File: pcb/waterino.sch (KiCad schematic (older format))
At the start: 40 parts, among them CON1 BARREL_JACK, IC1 ATMEGA168A-P, P1 CONN_02X02, P2 CONN_01X06, P3 CONN_01X07, P4 CONN_01X04, P5 CONN_01X07, SW1 SW_PUSH, U1 MAX6817, U2 LM7805CT, U3 MIC94090, Y1 Crystal

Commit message: wip
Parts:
- removed C8: 22pF, Capacitors_SMD:C_1206_HandSoldering, symbol C
- removed D6, D7: D, Diodes_ThroughHole:D_DO-41_SOD81_P7.62mm_Horizontal, symbol D
- removed IC1: ATMEGA168A-P, Housings_DIP:DIP-28_W7.62mm_Socket, symbol ATMEGA168A-P
- removed P2: CONN_01X06, Pin_Headers:Pin_Header_Straight_1x06_Pitch2.54mm, symbol CONN_01X06
- removed P3: CONN_01X07, Pin_Headers:Pin_Header_Angled_1x07_Pitch2.54mm, symbol CONN_01X07
- removed R10: 1M, Resistors_SMD:R_1206_HandSoldering, symbol R
- removed R6: 150R, Resistors_SMD:R_1206_HandSoldering, symbol R
- removed U1: MAX6817, TO_SOT_Packages_SMD:SOT-23-6_Handsoldering, symbol MAX6817
- removed Y1: Crystal, Crystals:Crystal_HC49-U_Vertical, symbol Crystal
- added C11: 100nF, Capacitors_SMD:C_1206_HandSoldering, symbol C
- added C12: 10nF, Capacitors_SMD:C_1206_HandSoldering, symbol C
- added D2: D_Schottky_AKA, TO_SOT_Packages_SMD:TO-252-2_Rectifier, symbol D_Schottky_AKA
- added D3, D5: D_Schottky, Diodes_SMD:D_SOD-123, symbol D_Schottky
- added J1: ICSP, Pin_Headers:Pin_Header_Straight_2x03_Pitch2.54mm, symbol CONN_02X03
- added J2: EXT_B, Pin_Headers:Pin_Header_Angled_1x06_Pitch2.54mm, symbol CONN_01X06
- added J3: EXT_A, Pin_Headers:Pin_Header_Angled_1x12_Pitch2.54mm, symbol CONN_01X12
- added R2: 4k7, Resistors_SMD:R_1206_HandSoldering, symbol R
- added R3, R4: 150, Resistors_SMD:R_1206_HandSoldering, symbol R
- added U3: ATMEGA168-20AU, Housings_QFP:TQFP-32_7x7mm_Pitch0.8mm, symbol ATMEGA168-20AU
- C6: value 10nF -> 100nF
- C9: value 22pF -> 100nF
- CON1: value BARREL_JACK -> POWER; footprint Connect:BARREL_JACK -> Connectors:BARREL_JACK
- D1: footprint Diodes_ThroughHole:D_DO-41_SOD81_P7.62mm_Horizontal -> Diodes_THT:D_DO-41_SOD81_P7.62mm_Horizontal
- D4: value LED -> PUMP_LED; symbol LED -> LED-RESCUE-waterino
- D6: renamed from D2; value LED -> RX_LED; symbol LED -> LED-RESCUE-waterino
- D7: renamed from D3; value LED -> TX_LED; symbol LED -> LED-RESCUE-waterino
- D8: renamed from D5; value LED -> PWR_LED; symbol LED -> LED-RESCUE-waterino
- P1: value CONN_02X02 -> PUMP
- P2: renamed from P5; value CONN_01X07 -> PLANT
- P3: renamed from P4; value CONN_01X04 -> UART
- R11: renamed from R7; value 150R -> 1.5K
- RL1: footprint Relays_ThroughHole:Relay_SPST_Finder_32.21-x300 -> Relays_THT:Relay_SPST_Finder_32.21-x300
- SW1: value SW_PUSH -> RESET; footprint Buttons_Switches_ThroughHole:SW_PUSH_6mm -> Buttons_Switches_THT:SW_PUSH_6mm
- renumbered R5 to R1, R2 to R10, R9 to R5, R8 to R6, R3 to R7, R4 to R8, R1 to R9, U2 to U1, U3 to U2
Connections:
- net XTAL2 is gone; now on net GND: C9.2
- net AVcc: now also C11.1, U3.18 (AVCC); no longer C7.1
- net AVss: now also C11.2, C12.2, U3.21 (GND); no longer C7.2
- net COIL_PWR: now also D3.1 (K)
- net EXT_A1: now also J2.2 (P2), U3.24 ((PCINT9/ADC1)PC1)
- net EXT_A2: now also J2.3 (P3), U3.19 (ADC6)
- net EXT_A3: now also J2.4 (P4), U3.22 (ADC7)
- net GND: now also C7.2, P2.7 (P7), SW1.1, D3.2 (A), J1.6 (P6), J2.6 (P6), J3.12 (P12), U3.3 (GND), U3.5 (GND); no longer C9.1, P2.3 (P3), R10.2, SW1.2
- net MOIST+: now also U3.25 ((PCINT10/ADC2)PC2)
- net MOIST-: now also P2.4 (P4), U3.27 ((PCINT12/SDA/ADC4)PC4); no longer P2.5 (P5)
- net MOISTURE: now also P2.3 (P3), U3.26 ((PCINT11/ADC3)PC3); no longer P2.6 (P6)
- net PGND: now also R10.2, D2.1 (A), D2.3 (A)
- net PUMP: now also U3.2 ((PCINT20/XCK/T0)PD4)
- net PUMP+: now also D2.2 (K)
- net REG_PWR: now also R11.1
- net RX: now also U3.30 ((PCINT16/RXD)PD0)
- net RX_LED: now also U3.9 ((PCINT21/OC0B/T1)PD5)
- net THERM: now also P2.5 (P5), U3.28 ((PCINT13/SCL/ADC5)PC5); no longer P2.1 (P1)
- net TX: now also U3.31 ((PCINT17/TXD)PD1)
- net TX_LED: now also U3.10 ((PCINT22/OC0A/AIN0)PD6)
- net Vcc: now also C7.1, C9.1, P2.1 (P1), D5.1 (K), J1.2 (P2), J2.5 (P5), J3.10 (P10), R2.2, U3.4 (VCC), U3.6 (VCC); no longer C6.1, P2.4 (P4)
- net ~OVRFLW: now also P2.6 (P6), U3.32 ((PCINT18/INT0)PD2); no longer P2.7 (P7)
- net LVL_SWTCH renamed ~LEVEL_ALERT
- net ~LEVEL_ALERT: now also U3.1 ((PCINT19/OC2B/INT1)PD3)
- new net: R3.1, SW1.2
- new net: R3.2, R4.1
- new net: C12.1, U3.20 (AREF)
- new net EXT_A0: J2.1 (P1), U3.23 ((PCINT8/ADC0)PC0)
- new net EXT_D0: J3.1 (P1), U3.12 ((PCINT0/CLKO/ICP1)PB0)
- new net EXT_D1: J3.2 (P2), U3.13 ((PCINT1/OC1A)PB1)
- new net EXT_D2: J3.3 (P3), U3.14 ((PCINT2/OC1B/~SS~)PB2)
- new net EXT_D6: J3.7 (P7), U3.7 ((PCINT6/XTAL1/TOSC1)PB6)
- new net EXT_D7: J3.8 (P8), U3.8 ((PCINT7/XTAL2/TOSC2)PB7)
- new net EXT_D8: J3.9 (P9), U3.11 ((PCINT23/AIN1)PD7)
- new net MISO: J1.1 (P1), J3.5 (P5), U3.16 ((PCINT4/MISO)PB4)
- new net MOSI: J1.4 (P4), J3.4 (P4), U3.15 ((PCINT3/OC2/MOSI)PB3)
- new net SCK: J1.3 (P3), J3.6 (P6), U3.17 ((PCINT5/SCK)PB5)
- new net ~RESET: C6.1, D5.2 (A), J1.5 (P5), J3.11 (P11), R2.1, R4.2, U3.29 ((PCINT14/~RESET~)PC6)
- no-connect marks 2 -> 1
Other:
- note added: "5V Load Summary:\nMCU: 2MHz@5V < 2mA active \nMoisture probe: 5V/10KR = 500µA\nOverflow sensor: 5V/100KR = 50µA when shorted \nLevel alert: 50µA when active (pullup from ground)\nThermal probe 10mA max when measuring.\nPump relay 40mA (nominal)\nPump LED max 2mA.\nMIC94090 20µA\nRX/TX should be low but max 40mA total\nRX/TX LED max 40mA total. \n\nTotal MAX: < 140 mA \nTypical Sleepl: < 100µA\nTy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"
- note added: "Green LED (2.2V, 20mA, 15mcd): We want 8mcd brightness: \n(12V -0.7V - 2.2V) / (20mA * 8mcd/15mcd) = 853 Ohm. \nPick 1.5K Ohm (E12, BOM reuse)."
- note added: "IC Max 20 µA \nNominal 40mA from relay"
- note added: "Level alert is debounced\nin software."
- note added: "Pot Connector\n(Moisture, Thermal and Overflow)"
- note added: "R3 forms a voltage voltage divider with the electrodes in the water. \nMy measurements put resistance of tap water at around 80-100k for\nsmall electrodes and around 2k for large electrodes (3cm galvanized screws).\nWe'll use large electrodes. The voltage at the divider when the electrodes \nare in water should be (internal pull-up disabled): \n\n Vcc * 2k / 102k = Vcc*0.02 which will trigger a l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"
- note added: "Recommended reset circuit\nfrom AVR HW considerations."
- note removed: "About max 300mA total drain before extension devices, typical 100mA\n during operation and the PWR LED will dominate when the µC is sleeping."
- note removed: "Debouncing"
- note removed: "Expansion Port A"
- note removed: "Expansion Port B"
- note removed: "Green LED (2.2V, 20mA, 15mcd): We want 8mcd brightness: \n(5V - 2.2V) / (20mA * 8mcd/15mcd) = 262 Ohm. \nPick 2x150 Ohm in series (E12)."
- note removed: "MCU will source at most 200mA from Vcc. \nPower LED will drain about 10mA\nRX/TX leds will drain about 40mA\nOverflow sensor if shorted will drain at most 50µA\nMoisture probe is included in MCU power. \nThermal probe will drain at most 10mA from Vcc."
- note removed: "Max 20 µA"
- note removed: "Max 20 µA + Nominal 40mA from relay"
- note removed: "Pot Molex\n(Moisture, Thermal Sensor and Overflow Detector)"
- note removed: "R3 forms a voltage voltage divider with the electrodes in the water. \nMy measurements put resistance of tap water at around 80-100k for\nsmall electrodes and around 2k for large electrodes (3cm galvanized screws).\nWe'll use large electrodes. The voltage at the divider when the electrodes \nare in water should be: \n\n Vcc * 2k / 102k = Vcc*0.02 which will trigger a level interrupt on INT0\n\nAT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"
- note removed: "UART Debugger"
- moved on the sheet: C1, C2, C3, C4, CON1, D1, D4, D6, D7, D8, P1, P2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

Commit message: Finally got it all together and ordered
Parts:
- removed J1: ICSP, Pin_Headers:Pin_Header_Straight_2x03_Pitch2.54mm, symbol CONN_02X03
- removed J2: EXT_B, Pin_Headers:Pin_Header_Angled_1x06_Pitch2.54mm, symbol CONN_01X06
- removed J3: EXT_A, Pin_Headers:Pin_Header_Angled_1x12_Pitch2.54mm, symbol CONN_01X12
- removed P2: PLANT, Connectors_JST:JST_PH_S7B-PH-K_07x2.00mm_Angled, symbol CONN_01X07
- added D9: D, Diodes_ThroughHole:D_DO-41_SOD81_P7.62mm_Horizontal, symbol D
- added F1: FUSE, Fuse_Holders_and_Fuses:Fuse_SMD2920, symbol FUSE
- added P2: PLANT, Connectors_JST:JST_PH_S6B-PH-K_06x2.00mm_Angled, symbol CONN_01X06
- added P4: CONN_02X06, Pin_Headers:Pin_Header_Straight_2x06_Pitch2.54mm, symbol CONN_02X06
- added P5: CONN_01X04, Pin_Headers:Pin_Header_Straight_2x02_Pitch2.54mm, symbol CONN_01X04
- added P6: CONN_01X03, Pin_Headers:Pin_Header_Straight_1x03_Pitch2.54mm, symbol CONN_01X03
- added R12: 5K11, Resistors_SMD:R_0603, symbol R
- added R13: 10K, Resistors_SMD:R_0603, symbol R
- C11, C12, C3, C4, C5, C6, C7, C9: footprint Capacitors_SMD:C_1206_HandSoldering -> Capacitors_SMD:C_0603
- D4, D6, D7, D8: footprint LEDs:LED_1206 -> LEDs:LED_0603
- R1: value 1.5k -> 1.5K; footprint Resistors_SMD:R_1206_HandSoldering -> Resistors_SMD:R_0603
- R10: value 0 -> 10K; footprint Resistors_SMD:R_1206_HandSoldering -> Resistors_SMD:R_0603
- R11, R3, R4: footprint Resistors_SMD:R_1206_HandSoldering -> Resistors_SMD:R_0603
- R2: value 4k7 -> 4K7; footprint Resistors_SMD:R_1206_HandSoldering -> Resistors_SMD:R_0603
- R5: value 100k -> 100K; footprint Resistors_SMD:R_1206_HandSoldering -> Resistors_SMD:R_0603
- R6: value 10k -> 10K; footprint Resistors_SMD:R_1206_HandSoldering -> Resistors_SMD:R_0603
- R7, R8: value 150R -> 150; footprint Resistors_SMD:R_1206_HandSoldering -> Resistors_SMD:R_0603
- R9: footprint Resistors_SMD:R_1206_HandSoldering -> Resistors_SMD:R_2010
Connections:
- net EXT_A0 is gone; now on net MOIST-: U3.23 ((PCINT8/ADC0)PC0)
- net EXT_A1 is gone; now on net MOIST+: U3.24 ((PCINT9/ADC1)PC1)
- net EXT_A2 is gone; now on net MOISTURE: U3.19 (ADC6)
- net EXT_A3 is gone; now on net THERM: U3.22 (ADC7)
- net +12V: now also F1.2; no longer CON1.1
- net AVcc: now also R5.2
- net EXT_D0: now also P4.11 (P11)
- net EXT_D1: now also P4.9 (P9)
- net EXT_D2: now also P4.7 (P7)
- net EXT_D6: now also P4.10 (P10)
- net EXT_D7: now also P4.8 (P8)
- net GND: now also C11.2, C12.2, R9.1, U3.21 (GND), P2.1 (P1), P2.6 (P6), P4.1 (P1), P5.4 (P4), P6.3 (P3); no longer P1.1 (P1), R9.2
- net MISO: now also P4.6 (P6)
- net MOIST+: now also R6.1; no longer R6.2, U3.25 ((PCINT10/ADC2)PC2)
- net MOIST-: now also P2.2 (P2); no longer U3.27 ((PCINT12/SDA/ADC4)PC4)
- net MOISTURE: now also R6.2, P2.3 (P3); no longer R6.1, U3.26 ((PCINT11/ADC3)PC3)
- net MOSI: now also P4.3 (P3)
- net PGND: now also P1.2 (P2), R9.2, R13.2; no longer R10.2, R9.1
- net PUMP: now also R1.1; no longer R1.2
- net RX_LED: now also U3.27 ((PCINT12/SDA/ADC4)PC4); no longer U3.9 ((PCINT21/OC0B/T1)PD5)
- net SCK: now also P4.4 (P4)
- net THERM: now also P2.4 (P4), R12.1; no longer U3.28 ((PCINT13/SCL/ADC5)PC5)
- net TX_LED: now also U3.28 ((PCINT13/SCL/ADC5)PC5); no longer U3.10 ((PCINT22/OC0A/AIN0)PD6)
- net Vcc: now also R10.1, P4.12 (P12), P4.5 (P5), P6.1 (P1); no longer R5.1
- net ~LEVEL_ALERT: now also R10.2, U3.26 ((PCINT11/ADC3)PC3), D9.2 (A); no longer P1.2 (P2), U3.1 ((PCINT19/OC2B/INT1)PD3)
- net ~OVRFLW: now also R5.1, P2.5 (P5); no longer R5.2
- net ~RESET: now also P4.2 (P2)
- net at D4.2 (A): now also R1.2; no longer R1.1
- removed net AVss: C11.2, C12.2, R10.1, U3.21 (GND)
- net EXT_D8 renamed BUZZER
- net BUZZER: now also P5.2 (P2)
- new net: D9.1 (K), P1.1 (P1), R13.1
- new net INT1: P6.2 (P2), U3.1 ((PCINT19/OC2B/INT1)PD3)
- new net LEVEL_LED: P5.3 (P3), U3.10 ((PCINT22/OC0A/AIN0)PD6)
- new net PWR: CON1.1, F1.1
- new net SHORT_LED: P5.1 (P1), U3.9 ((PCINT21/OC0B/T1)PD5)
- new net THERM+: R12.2, U3.25 ((PCINT10/ADC2)PC2)
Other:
- note added: "5V Load Summary:\n - MCU: 1MHz@5V (internal RC) < 1mA active \n - Moisture probe: 5V/10KR = 500µA (when shorted)\n - Overflow sensor: 5V/100KR = 50µA (when shorted)\n - Level alert: 50µA when active (pullup from ground)\n - Thermal probe 1mA (when shorted)\n - Pump relay 40mA (nominal)\n - MIC94090 20µA\n - Pump LED max 2mA.\n - RX/TX should be low but max 40mA total\n - RX/TX LED max 40mA total.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"
- note added: "750mW max"
- note added: "C7 near pins 4 and 3"
- note added: "C9 near pins 5 and 6"
- note added: "Failure analysis P1:\nPin: ~LEVEL_ALERT:\n - May short to GND or PGND, both are equivalent to\n level alert triggering normally.\n - May short to +12V. Diode becomes reverse biased\n and level_alert goes to 5V. \n\nPin: 12V\n - May short to PGND, fuse will trip.\n - May short to GND, fuse will trip. May damage traces \n and zero ohm resistor between GND and PGND.\nPin: PGND\n - May short to GND. 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"
- note added: "Green LED (2.2V, 20mA, 15mcd): \nWe want 8mcd brightness: \n(12V -0.7V - 2.2V) / (20mA * 8mcd/15mcd) = 853 Ohm. \nPick 1.5K Ohm (E12, BOM reuse)."
- note added: "LM78M05CT - http://uk.farnell.com/fairchild-semiconductor/lm78m05ct/ic-v-reg-5v-0-5a-3to220/dp/1417671\nMF-LSMF300/24X - http://uk.farnell.com/bourns/lsmf300-24x-2/fuse-resettable-ptc-24v-3a-2920/dp/2057925"
- note added: "MOIST+ and MOIST- are normally tristate.\nWhen measuring + is driven high and - is driven low causing a current to flow through\nR6 and the soil (two electrodes connected between pin 2 and 3 of P2). Then the polarity\nis reversed to counteract electron migration on the electrodes.\nThe voltage at the divider is measured using ADC. \nR6 is chosen based on earlier experiments for the designed targe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"
- note added: "Vcc = 5 ±0.36V"
- note removed: "5V Load Summary:\nMCU: 2MHz@5V < 2mA active \nMoisture probe: 5V/10KR = 500µA\nOverflow sensor: 5V/100KR = 50µA when shorted \nLevel alert: 50µA when active (pullup from ground)\nThermal probe 10mA max when measuring.\nPump relay 40mA (nominal)\nPump LED max 2mA.\nMIC94090 20µA\nRX/TX should be low but max 40mA total\nRX/TX LED max 40mA total. \n\nTotal MAX: < 140 mA \nTypical Sleepl: < 100µA\nTy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"
- note removed: "Green LED (2.2V, 20mA, 15mcd): We want 8mcd brightness: \n(12V -0.7V - 2.2V) / (20mA * 8mcd/15mcd) = 853 Ohm. \nPick 1.5K Ohm (E12, BOM reuse)."
- note removed: "Pot Connector\n(Moisture, Thermal and Overflow)"
- note removed: "R3 forms a voltage voltage divider with the electrodes in the water. \nMy measurements put resistance of tap water at around 80-100k for\nsmall electrodes and around 2k for large electrodes (3cm galvanized screws).\nWe'll use large electrodes. The voltage at the divider when the electrodes \nare in water should be (internal pull-up disabled): \n\n Vcc * 2k / 102k = Vcc*0.02 which will trigger a l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"
- note removed: "Reservoir Molex\n(Pump Power and Water Level Alert)"
- moved on the sheet: C1, C11, C12, C2, C3, C4, C5, C6, C7, C9, CON1, D1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

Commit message: Adding libraries and cleaning up some more.
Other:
- note removed: "LM78M05CT - http://uk.farnell.com/fairchild-semiconductor/lm78m05ct/ic-v-reg-5v-0-5a-3to220/dp/1417671\nMF-LSMF300/24X - http://uk.farnell.com/bourns/lsmf300-24x-2/fuse-resettable-ptc-24v-3a-2920/dp/2057925"
- moved on the sheet: C1, C11, C12, C2, C3, C4, C5, C6, C7, C9, CON1, D1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

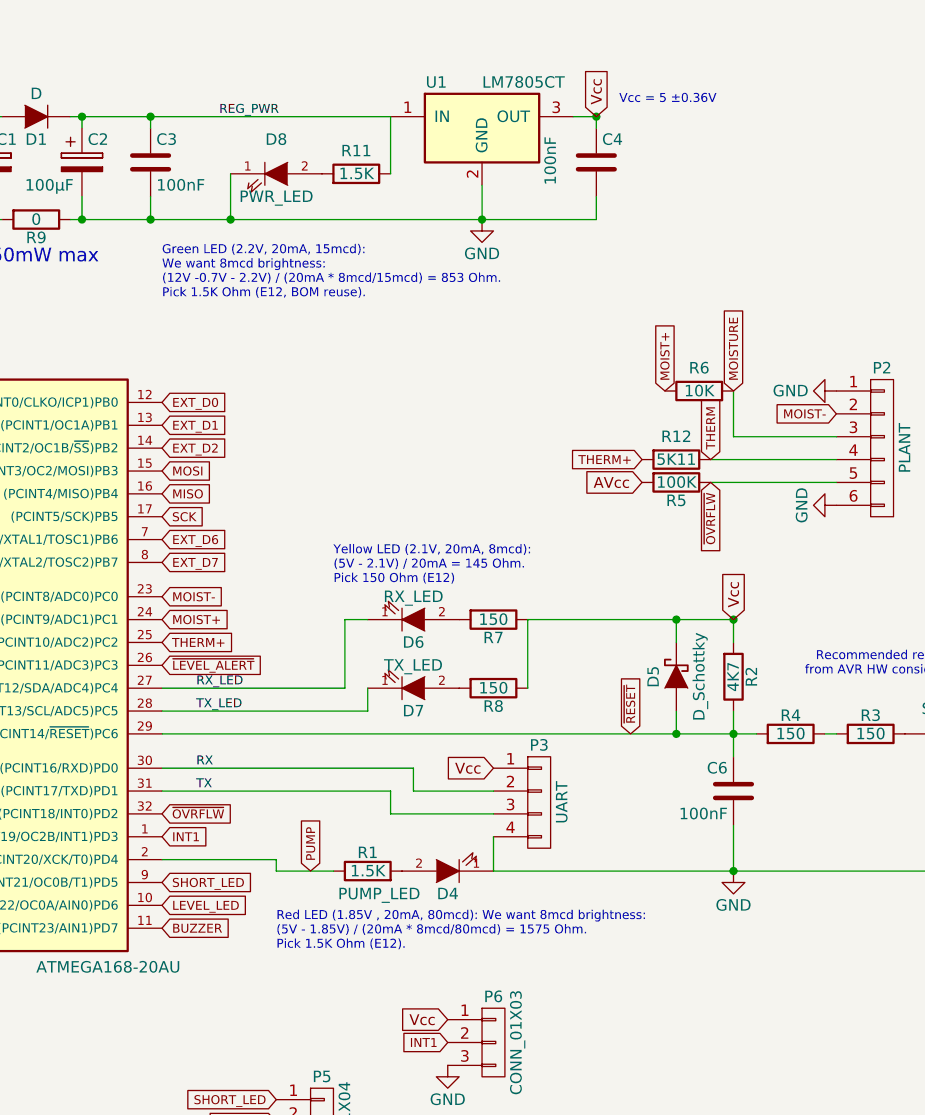
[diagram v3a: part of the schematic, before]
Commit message: Fixing compile issues and adding a self-test program to test soldering connections on a new waterino.
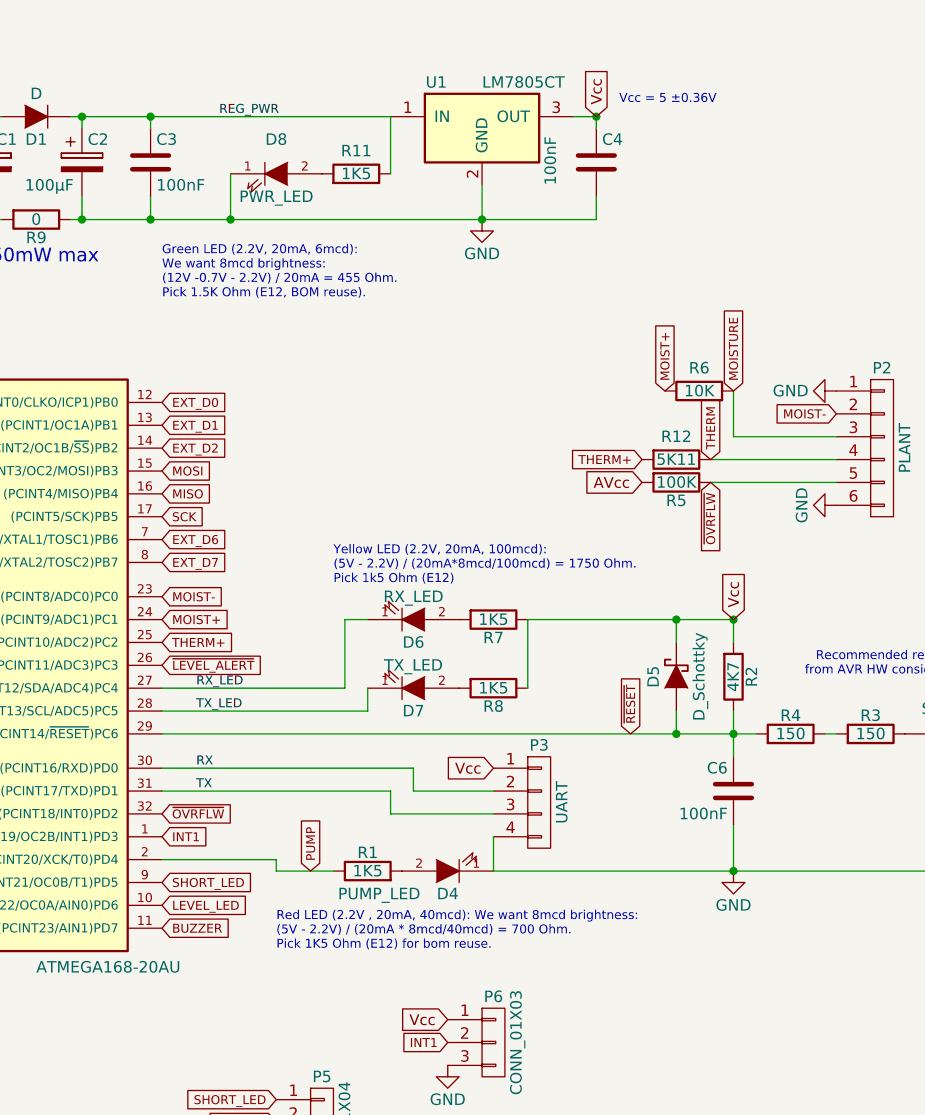
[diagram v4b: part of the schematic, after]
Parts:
- R1, R11: value 1.5K -> 1K5
- R7, R8: value 150 -> 1K5
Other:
- note added: "Green LED (2.2V, 20mA, 6mcd): \nWe want 8mcd brightness: \n(12V -0.7V - 2.2V) / 20mA = 455 Ohm. \nPick 1.5K Ohm (E12, BOM reuse)."
- note added: "Red LED (2.2V , 20mA, 40mcd): We want 8mcd brightness:\n(5V - 2.2V) / (20mA * 8mcd/40mcd) = 700 Ohm.\nPick 1K5 Ohm (E12) for bom reuse."
- note added: "Yellow LED (2.2V, 20mA, 100mcd): \n(5V - 2.2V) / (20mA*8mcd/100mcd) = 1750 Ohm.\nPick 1k5 Ohm (E12)"
- note removed: "Green LED (2.2V, 20mA, 15mcd): \nWe want 8mcd brightness: \n(12V -0.7V - 2.2V) / (20mA * 8mcd/15mcd) = 853 Ohm. \nPick 1.5K Ohm (E12, BOM reuse)."
- note removed: "Red LED (1.85V , 20mA, 80mcd): We want 8mcd brightness:\n(5V - 1.85V) / (20mA * 8mcd/80mcd) = 1575 Ohm.\nPick 1.5K Ohm (E12)."
- note removed: "Yellow LED (2.1V, 20mA, 8mcd): \n(5V - 2.1V) / 20mA = 145 Ohm.\nPick 150 Ohm (E12)"
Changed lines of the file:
@@
 F 1 "PWR_LED" H 4750 2900 50  0000 C CNN
 F 2 "LEDs:LED_0603" H 4750 3000 50  0001 C CNN
-F 3 "" H 4750 3000 50  0000 C CNN
+F 3 "http://www.rohm.com/web/global/datasheet/SML-D12V8W" H 4750 3000 50  0001 C CNN
 	1    4750 3000
 	1    0    0    -1
@@
 P 5150 6050
 F 0 "R1" V 5230 6050 50  0000 C CNN
-F 1 "1.5K" V 5150 6050 50  0000 C CNN
+F 1 "1K5" V 5150 6050 50  0000 C CNN
 F 2 "Resistors_SMD:R_0603" V 5080 6050 50  0001 C CNN
 F 3 "" H 5150 6050 50  0000 C CNN
@@
 F 1 "PUMP_LED" H 5800 6150 50  0000 C CNN
 F 2 "LEDs:LED_0603" H 5500 6050 50  0001 C CNN
-F 3 "" H 5500 6050 50  0000 C CNN
+F 3 "http://www.rohm.com/web/global/datasheet/SML-D12V8W" H 5500 6050 50  0001 C CNN
 	1    5500 6050
 	-1   0    0    1
@@
 P 5700 5250
 F 0 "R8" V 5780 5250 50  0000 C CNN
-F 1 "150" V 5700 5250 50  0000 C CNN
+F 1 "1K5" V 5700 5250 50  0000 C CNN
 F 2 "Resistors_SMD:R_0603" V 5630 5250 50  0001 C CNN
 F 3 "" H 5700 5250 50  0000 C CNN
@@
 F 1 "TX_LED" H 5350 5150 50  0000 C CNN
 F 2 "LEDs:LED_0603" H 5350 5250 50  0001 C CNN
-F 3 "" H 5350 5250 50  0000 C CNN
+F 3 "http://www.rohm.com/web/global/datasheet/SML-D12V8W" H 5350 5250 50  0001 C CNN
 	1    5350 5250
 	1    0    0    1
@@
 F 1 "RX_LED" H 5350 4850 50  0000 C CNN
 F 2 "LEDs:LED_0603" H 5350 4950 50  0001 C CNN
-F 3 "" H 5350 4950 50  0000 C CNN
+F 3 "http://www.rohm.com/web/global/datasheet/SML-D12V8W" H 5350 4950 50  0001 C CNN
 	1    5350 4950
 	1    0    0    1
@@
 P 5700 4950
 F 0 "R7" V 5780 4950 50  0000 C CNN
-F 1 "150" V 5700 4950 50  0000 C CNN
+F 1 "1K5" V 5700 4950 50  0000 C CNN
 F 2 "Resistors_SMD:R_0603" V 5630 4950 50  0001 C CNN
 F 3 "" H 5700 4950 50  0000 C CNN
@@
 Vcc
 Text Notes 5000 4800 0    39   ~ 0
-Yellow LED (2.1V, 20mA, 8mcd): \n(5V - 2.1V) / 20mA = 145 Ohm.\nPick 150 Ohm (E12)
+Yellow LED (2.2V, 20mA, 100mcd): \n(5V - 2.2V) / (20mA*8mcd/100mcd) = 1750 Ohm.\nPick 1k5 Ohm (E12)
 Text Notes 4250 3550 0    39   ~ 0
-Green LED (2.2V, 20mA, 15mcd): \nWe want 8mcd brightness: \n(12V -0.7V - 2.2V) / (20mA * 8mcd/15mcd) = 853 Ohm.  \nPick 1.5K Ohm (E12, BOM reuse).
+Green LED (2.2V, 20mA, 6mcd): \nWe want 8mcd brightness: \n(12V -0.7V - 2.2V) / 20mA = 455 Ohm.  \nPick 1.5K Ohm (E12, BOM reuse).
 Text Notes 7700 4650 0    39   ~ 0
 MOIST+ and MOIST- are normally tristate.\nWhen measuring + is driven high and - is driven low causing a current to flow through\nR6 and the soil (two electrodes connected between pin 2 and 3 of P2). Then the polarity\nis reversed to counteract electron migration on the electrodes.\nThe voltage at the divider is measured using ADC. \nR6 is chosen based on earlier experiments for the designed target soil. \n\nBetween pins 5 and 6 of P2 are two electrodes that short if the pot overflows with water.\nR5 forms a series resistance with the electrodes and is weakly pulled high.  The value for\nR5 is chosen based on measured resistance of tap water with large electrodes.\nThe resistance measured was around 2k for 3cm galvanized screws submerged\nin water. The expected voltage on INT0 when in water is 0.02*Vcc. Internal pull-up\nmust be disabled. An IRQ will trigger up to 72k resistance between the probes. \n(ATmega has 2.6V input threshold on pins and .5V hysteresis)\n\n\nR12 likewise forms a voltage divider but with a thermistor, the datasheet suggest a \n5k11 series resistor to linearise the thermistor. We use THERM+ to drive the divider\nwhen we want to measure. Otherwise THERM+ is tristate. 5V/5K = 1mA which the GPIO\npin can easily drive.
 Text Notes 4750 6400 0    39   ~ 0
-Red LED (1.85V , 20mA, 80mcd): We want 8mcd brightness:\n(5V - 1.85V) / (20mA * 8mcd/80mcd) = 1575 Ohm.\nPick 1.5K Ohm (E12).
+Red LED (2.2V , 20mA, 40mcd): We want 8mcd brightness:\n(5V - 2.2V) / (20mA * 8mcd/40mcd) = 700 Ohm.\nPick 1K5 Ohm (E12) for bom reuse.
 $Comp
 L D D1
@@
 P 5100 3000
 F 0 "R11" V 5200 3000 50  0000 C CNN
-F 1 "1.5K" V 5100 3000 50  0000 C CNN
+F 1 "1K5" V 5100 3000 50  0000 C CNN
 F 2 "Resistors_SMD:R_0603" V 5030 3000 50  0001 C CNN
 F 3 "" H 5100 3000 50  0000 C CNN
